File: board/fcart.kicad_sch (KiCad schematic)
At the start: 110 parts, among them J1 USB4085, J2 MSD-4-A, J3 SWD, J4 JTAG, J5 Famicom_cartridge, Q1 DTC114E, SW1 PTS647SM70, U1 USBLC6-2SC6, U10 W9864G6KH-6, U2 TLV76133DCY, U3 MCP6001, U4 SN74ALVC164245DGG, U5 SN74ALVC164245DGG, U6 SN74ALVC164245DGG, U7 SN74ALVC164245DGG, U8 STM32F412RET6, U9 LCMXO2-4000HC-4TG144C, Y1 ABS07-32.768KHZ-7, Y2 ABM8W-12.0000MHZ-8-B1U, Y3 ASE-50.000MHZ-LC

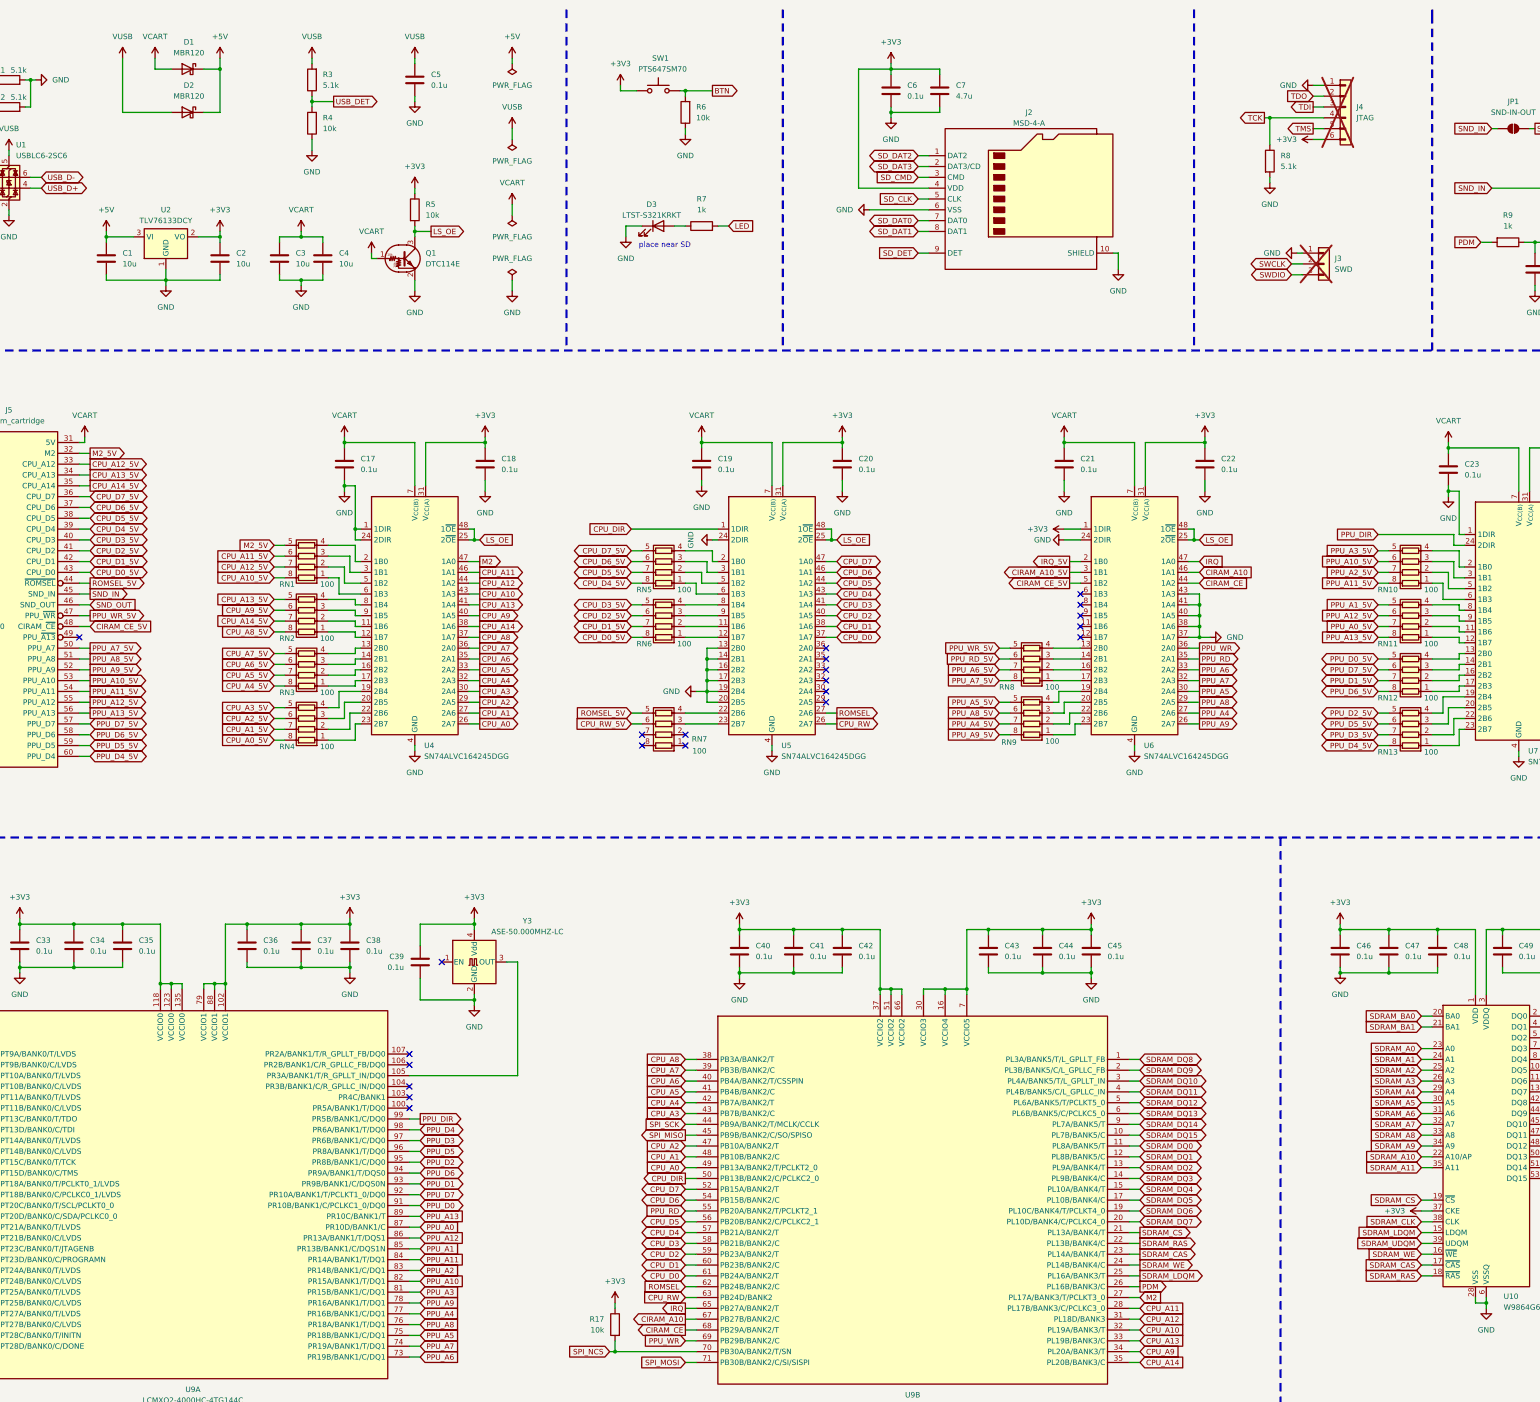
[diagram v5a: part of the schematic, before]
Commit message: pcb: Fix USB backpowering to the console through level shifters
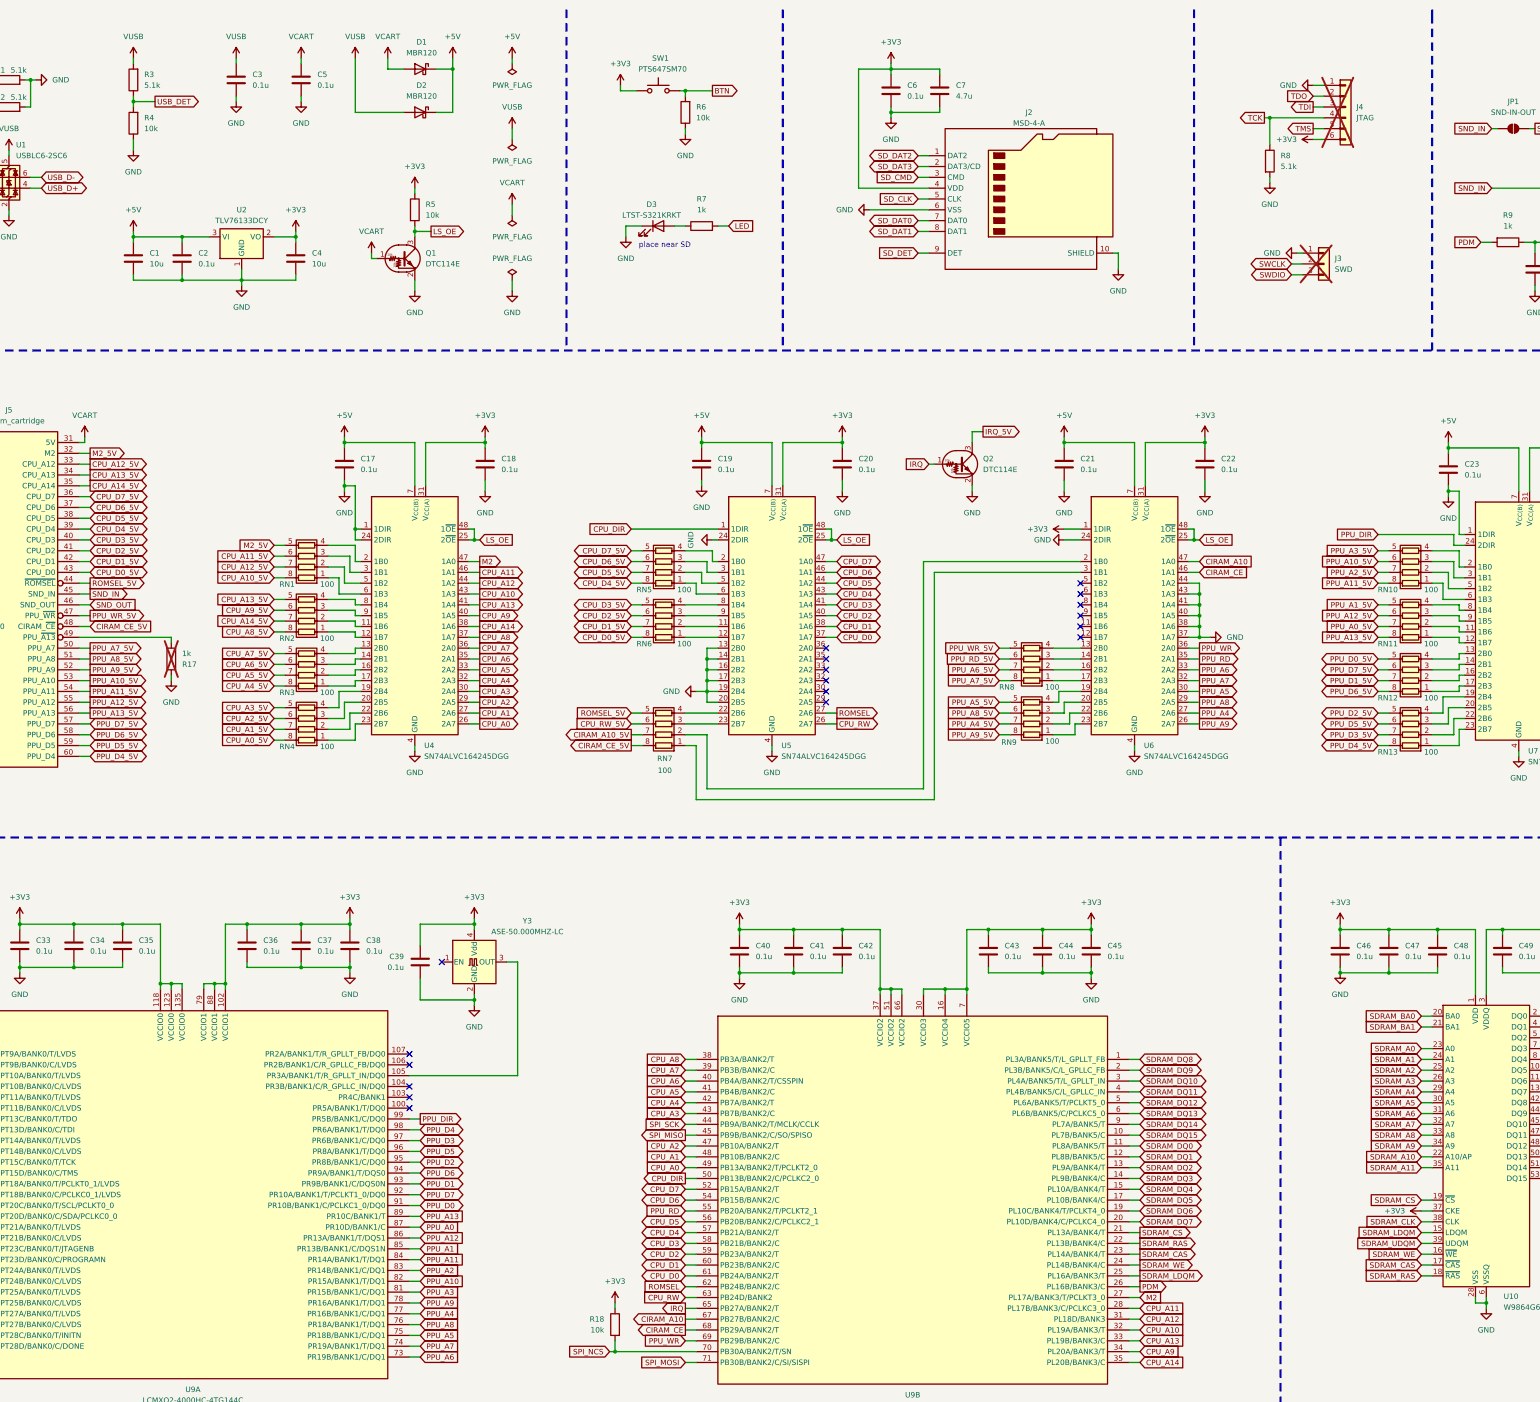
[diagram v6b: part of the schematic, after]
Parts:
- removed C4: 10u, Capacitor_SMD:C_0805_2012Metric, symbol Device:C
- added C2: 0.1u, Capacitor_SMD:C_0805_2012Metric, symbol Device:C
- added Q2: DTC114E, Package_TO_SOT_SMD:SOT-23-3, symbol Transistor_BJT:DTC114E
- added R17: 1k, Resistor_SMD:R_0805_2012Metric, symbol Device:R
- C5: renamed from C3; value 10u -> 0.1u
- renumbered C5 to C3, C2 to C4, R17 to R18
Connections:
- net +5V: now also C17.1, C19.1, C21.1, C23.1, U4.18 (V_{CC(B)}), U4.7 (V_{CC(B)}), U5.18 (V_{CC(B)}), U5.7 (V_{CC(B)}), U6.18 (V_{CC(B)}), U6.7 (V_{CC(B)}), U7.18 (V_{CC(B)}), U7.7 (V_{CC(B)}), C2.1
- net CIRAM_A10: now also U6.47 (1A0); no longer U6.46 (1A1)
- net CIRAM_A10_5V: now also RN7.7 (R2.2); no longer U6.3 (1B1)
- net CIRAM_CE: now also U6.46 (1A1); no longer U6.44 (1A2)
- net CIRAM_CE_5V: now also RN7.8 (R1.2); no longer U6.5 (1B2)
- net GND: now also U6.44 (1A2), C2.2, Q2.2 (E), R17.1
- net IRQ: now also Q2.1 (B); no longer U6.47 (1A0)
- net IRQ_5V: now also Q2.3 (C); no longer U6.2 (1B0)
- net VCART: no longer C17.1, C19.1, C21.1, C23.1, U4.18 (V_{CC(B)}), U4.7 (V_{CC(B)}), U5.18 (V_{CC(B)}), U5.7 (V_{CC(B)}), U6.18 (V_{CC(B)}), U6.7 (V_{CC(B)}), U7.18 (V_{CC(B)}), U7.7 (V_{CC(B)})
- net at RN7.1 (R1.1): now also U6.3 (1B1)
- net at RN7.2 (R2.1): now also U6.2 (1B0)
- net at J5.49 (PPU_~{A13}): now also R17.2
- no-connect marks 46 -> 42
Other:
- moved on the sheet: C1, C3, C4, C5, D1, D2, R3, R4, U2
